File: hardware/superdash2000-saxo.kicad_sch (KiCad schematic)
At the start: 3 parts

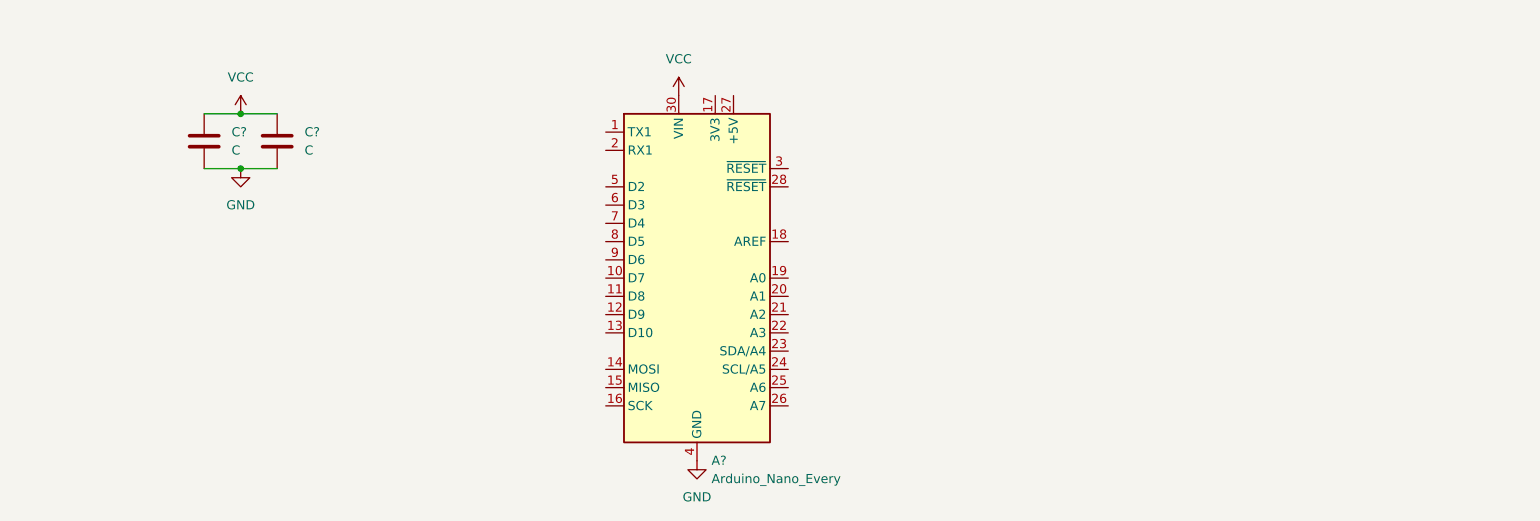
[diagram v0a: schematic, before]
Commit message: hardware: Add LDO and modify PCB
Signed-off-by: Thomas Antonini <antonini.thomas@gmail.com>
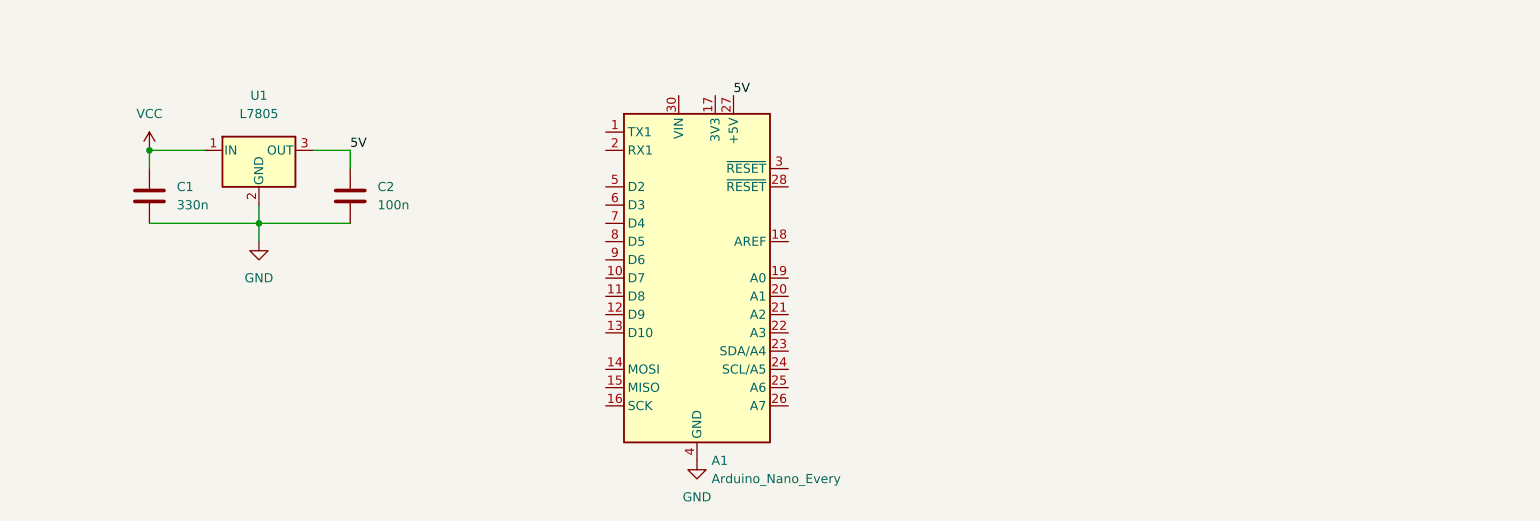
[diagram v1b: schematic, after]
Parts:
- removed C?: C, symbol Device:C
- added C2: 100n, Capacitor_THT:C_Disc_D3.0mm_W1.6mm_P2.50mm, symbol Device:C
- added U1: L7805, Package_TO_SOT_THT:TO-220-3_Vertical, symbol Regulator_Linear:L7805
- C1: renamed from C?; value C -> 330n; footprint (none) -> Capacitor_THT:C_Disc_D3.0mm_W1.6mm_P2.50mm
- gave numbers to parts that had none: 1
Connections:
- net GND: now also C2.2, U1.2 (GND)
- net VCC: now also U1.1 (IN); no longer A1.30 (VIN)
- net 5V: now reaches A1.27 (+5V)
- net 5V: now also C2.1, U1.3 (OUT)
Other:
- moved on the sheet: C1
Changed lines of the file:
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@@
 (kicad_sch (version 20211123) (generator eeschema)
   (paper "A4")
-  (junction (at 59.69 54.61) (diameter 0) (color 0 0 0 0)
+  (junction (at 46.99 59.69) (diameter 0) (color 0 0 0 0)
   )
-  (junction (at 59.69 62.23) (diameter 0) (color 0 0 0 0)
+  (junction (at 62.23 69.85) (diameter 0) (color 0 0 0 0)
   )
-  (wire (pts (xy 54.61 62.23) (xy 59.69 62.23))
+  (wire (pts (xy 62.23 69.85) (xy 62.23 72.39))
     (stroke (width 0) (type default) (color 0 0 0 0))
   )
-  (wire (pts (xy 59.69 62.23) (xy 64.77 62.23))
+  (wire (pts (xy 62.23 69.85) (xy 74.93 69.85))
     (stroke (width 0) (type default) (color 0 0 0 0))
   )
-  (wire (pts (xy 59.69 54.61) (xy 64.77 54.61))
+  (wire (pts (xy 62.23 67.31) (xy 62.23 69.85))
     (stroke (width 0) (type default) (color 0 0 0 0))
   )
-  (wire (pts (xy 54.61 54.61) (xy 59.69 54.61))
+  (wire (pts (xy 46.99 69.85) (xy 62.23 69.85))
     (stroke (width 0) (type default) (color 0 0 0 0))
+  )
+  (wire (pts (xy 74.93 59.69) (xy 69.85 59.69))
+    (stroke (width 0) (type default) (color 0 0 0 0))
+  )
+  (wire (pts (xy 74.93 62.23) (xy 74.93 59.69))
+    (stroke (width 0) (type default) (color 0 0 0 0))
+  )
+  (wire (pts (xy 46.99 59.69) (xy 54.61 59.69))
+    (stroke (width 0) (type default) (color 0 0 0 0))
+  )
+  (wire (pts (xy 46.99 59.69) (xy 46.99 62.23))
+    (stroke (width 0) (type default) (color 0 0 0 0))
+  )
+  (label "5V" (at 74.93 59.69 0)
+    (effects (font (size 1.27 1.27)) (justify left bottom))
+  )
+  (label "5V" (at 128.27 52.07 0)
+    (effects (font (size 1.27 1.27)) (justify left bottom))
   )
   (symbol (lib_id "power:GND") (at 123.19 102.87 0) (unit 1)
     (in_bom yes) (on_board yes) (fields_autoplaced)
-    (property "Reference" "#PWR?" (id 0) (at 123.19 109.22 0)
+    (property "Reference" "#PWR0101" (id 0) (at 123.19 109.22 0)
       (effects (font (size 1.27 1.27)) hide)
     )
@@
     (pin "1")
   )
-  (symbol (lib_id "power:GND") (at 59.69 62.23 0) (unit 1)
+  (symbol (lib_id "power:GND") (at 62.23 72.39 0) (unit 1)
     (in_bom yes) (on_board yes) (fields_autoplaced)
-    (property "Reference" "#PWR?" (id 0) (at 59.69 68.58 0)
+    (property "Reference" "#PWR0102" (id 0) (at 62.23 78.74 0)
       (effects (font (size 1.27 1.27)) hide)
     )
-    (property "Value" "GND" (id 1) (at 59.69 67.31 0))
-    (property "Footprint" "" (id 2) (at 59.69 62.23 0)
+    (property "Value" "GND" (id 1) (at 62.23 77.47 0))
+    (property "Footprint" "" (id 2) (at 62.23 72.39 0)
       (effects (font (size 1.27 1.27)) hide)
     )
-    (property "Datasheet" "" (id 3) (at 59.69 62.23 0)
+    (property "Datasheet" "" (id 3) (at 62.23 72.39 0)
       (effects (font (size 1.27 1.27)) hide)
     )
     (pin "1")
   )
-  (symbol (lib_id "Device:C") (at 64.77 58.42 0) (unit 1)
-    (in_bom yes) (on_board yes) (fields_autoplaced)
-    (property "Reference" "C?" (id 0) (at 68.58 57.1499 0)
+  (symbol (lib_id "Device:C") (at 74.93 66.04 0) (unit 1)
+    (in_bom yes) (on_board yes)
+    (property "Reference" "C2" (id 0) (at 78.74 64.7699 0)
       (effects (font (size 1.27 1.27)) (justify left))
     )
-    (property "Value" "C" (id 1) (at 68.58 59.6899 0)
+    (property "Value" "100n" (id 1) (at 78.74 67.3099 0)
       (effects (font (size 1.27 1.27)) (justify left))
     )
-    (property "Footprint" "" (id 2) (at 65.7352 62.23 0)
+    (property "Footprint" "Capacitor_THT:C_Disc_D3.0mm_W1.6mm_P2.50mm" (id 2) (at 75.8952 69.85 0)
       (effects (font (size 1.27 1.27)) hide)
     )
-    (property "Datasheet" "~" (id 3) (at 64.77 58.42 0)
+    (property "Datasheet" "~" (id 3) (at 74.93 66.04 0)
       (effects (font (size 1.27 1.27)) hide)
     )
@@
     (pin "2")
   )
+  (symbol (lib_id "Regulator_Linear:L7805") (at 62.23 59.69 0) (unit 1)
+    (in_bom yes) (on_board yes) (fields_autoplaced)
+    (property "Reference" "U1" (id 0) (at 62.23 52.07 0))
+    (property "Value" "L7805" (id 1) (at 62.23 54.61 0))
+    (property "Footprint" "Package_TO_SOT_THT:TO-220-3_Vertical" (id 2) (at 62.865 63.5 0)
+      (effects (font (size 1.27 1.27) italic) (justify left) hide)
+    )
+    (property "Datasheet" "http://www.st.com/content/ccc/resource/technical/document/datasheet/41/4f/b3/b0/12/d4/47/88/CD00000444.pdf/files/CD00000444.pdf/jcr:content/translations/en.CD00000444.pdf" (id 3) (at 62.23 60.96 0)
+      (effects (font (size 1.27 1.27)) hide)
+    )
+    (pin "1")
+    (pin "2")
+    (pin "3")
+  )
   (symbol (lib_id "MCU_Module:Arduino_Nano_Every") (at 123.19 77.47 0) (unit 1)
     (in_bom yes) (on_board yes) (fields_autoplaced)
-    (property "Reference" "A?" (id 0) (at 125.2094 102.87 0)
+    (property "Reference" "A1" (id 0) (at 125.2094 102.87 0)
       (effects (font (size 1.27 1.27)) (justify left))
     )
@@
     (pin "9")
   )
-  (symbol (lib_id "power:VCC") (at 120.65 52.07 0) (unit 1)
-    (in_bom yes) (on_board yes) (fields_autoplaced)
-    (property "Reference" "#PWR?" (id 0) (at 120.65 55.88 0)
+  (symbol (lib_id "Device:C") (at 46.99 66.04 0) (unit 1)
+    (in_bom yes) (on_board yes)
+    (property "Reference" "C1" (id 0) (at 50.8 64.7699 0)
+      (effects (font (size 1.27 1.27)) (justify left))
+    )
+    (property "Value" "330n" (id 1) (at 50.8 67.3099 0)
+      (effects (font (size 1.27 1.27)) (justify left))
+    )
+    (property "Footprint" "Capacitor_THT:C_Disc_D3.0mm_W1.6mm_P2.50mm" (id 2) (at 47.9552 69.85 0)
       (effects (font (size 1.27 1.27)) hide)
     )
-    (property "Value" "VCC" (id 1) (at 120.65 46.99 0))
-    (property "Footprint" "" (id 2) (at 120.65 52.07 0)
-      (effects (font (size 1.27 1.27)) hide)
-    )
-    (property "Datasheet" "" (id 3) (at 120.65 52.07 0)
-      (effects (font (size 1.27 1.27)) hide)
-    )
-    (pin "1")
-  )
-  (symbol (lib_id "Device:C") (at 54.61 58.42 0) (unit 1)
-    (in_bom yes) (on_board yes) (fields_autoplaced)
-    (property "Reference" "C?" (id 0) (at 58.42 57.1499 0)
-      (effects (font (size 1.27 1.27)) (justify left))
-    )
-    (property "Value" "C" (id 1) (at 58.42 59.6899 0)
-      (effects (font (size 1.27 1.27)) (justify left))
-    )
-    (property "Footprint" "" (id 2) (at 55.5752 62.23 0)
-      (effects (font (size 1.27 1.27)) hide)
-    )
-    (property "Datasheet" "~" (id 3) (at 54.61 58.42 0)
+    (property "Datasheet" "~" (id 3) (at 46.99 66.04 0)
       (effects (font (size 1.27 1.27)) hide)
     )
@@
     (pin "2")
   )
-  (symbol (lib_id "power:VCC") (at 59.69 54.61 0) (unit 1)
+  (symbol (lib_id "power:VCC") (at 46.99 59.69 0) (unit 1)
     (in_bom yes) (on_board yes) (fields_autoplaced)
-    (property "Reference" "#PWR?" (id 0) (at 59.69 58.42 0)
+    (property "Reference" "#PWR0103" (id 0) (at 46.99 63.5 0)
       (effects (font (size 1.27 1.27)) hide)
     )
-    (property "Value" "VCC" (id 1) (at 59.69 49.53 0))
-    (property "Footprint" "" (id 2) (at 59.69 54.61 0)
+    (property "Value" "VCC" (id 1) (at 46.99 54.61 0))
+    (property "Footprint" "" (id 2) (at 46.99 59.69 0)
       (effects (font (size 1.27 1.27)) hide)
     )
-    (property "Datasheet" "" (id 3) (at 59.69 54.61 0)
+    (property "Datasheet" "" (id 3) (at 46.99 59.69 0)
       (effects (font (size 1.27 1.27)) hide)
     )
@@
   (symbol_instances
     (path "/091fa7fe-31f2-4bc7-b9ae-103378e7ecef"
-      (reference "#PWR?") (unit 1) (value "GND") (footprint "")
+      (reference "#PWR0101") (unit 1) (value "GND") (footprint "")
     )
     (path "/2d42965a-3076-4350-a25e-4a3c6a2ed82a"
-      (reference "#PWR?") (unit 1) (value "GND") (footprint "")
-    )
-    (path "/c516dcf8-f4c1-4011-b67e-724a30d35ccf"
-      (reference "#PWR?") (unit 1) (value "VCC") (footprint "")
+      (reference "#PWR0102") (unit 1) (value "GND") (footprint "")
     )
     (path "/f16717c9-4da6-4641-a01d-d15d2a023c10"
-      (reference "#PWR?") (unit 1) (value "VCC") (footprint "")
+      (reference "#PWR0103") (unit 1) (value "VCC") (footprint "")
     )
     (path "/65c02b6a-4170-4a63-9193-eec01920d5e8"
-      (reference "A?") (unit 1) (value "Arduino_Nano_Every") (footprint "Module:Arduino_Nano")
-    )
-    (path "/4f6c1128-a97e-4ba7-b96b-87bbab886b6c"
-      (reference "C?") (unit 1) (value "C") (footprint "")
+      (reference "A1") (unit 1) (value "Arduino_Nano_Every") (footprint "Module:Arduino_Nano")
     )
     (path "/eae34f3b-9c4a-4c30-981e-9737d2460a8b"
-      (reference "C?") (unit 1) (value "C") (footprint "")
+      (reference "C1") (unit 1) (value "330n") (footprint "Capacitor_THT:C_Disc_D3.0mm_W1.6mm_P2.50mm")
+    )
+    (path "/42e4bc1f-a2a4-4278-9288-7ff8c44f13b1"
+      (reference "C2") (unit 1) (value "100n") (footprint "Capacitor_THT:C_Disc_D3.0mm_W1.6mm_P2.50mm")
+    )
+    (path "/4dcd0dda-1663-4b04-85dd-f6fe52c14280"
+      (reference "U1") (unit 1) (value "L7805") (footprint "Package_TO_SOT_THT:TO-220-3_Vertical")
     )
   )

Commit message: hardware: Update schematics
Add fuse
Add 3-pin jumper
Add molex connector
Move symbols position

Signed-off-by: Thomas Antonini <antonini.thomas@gmail.com>
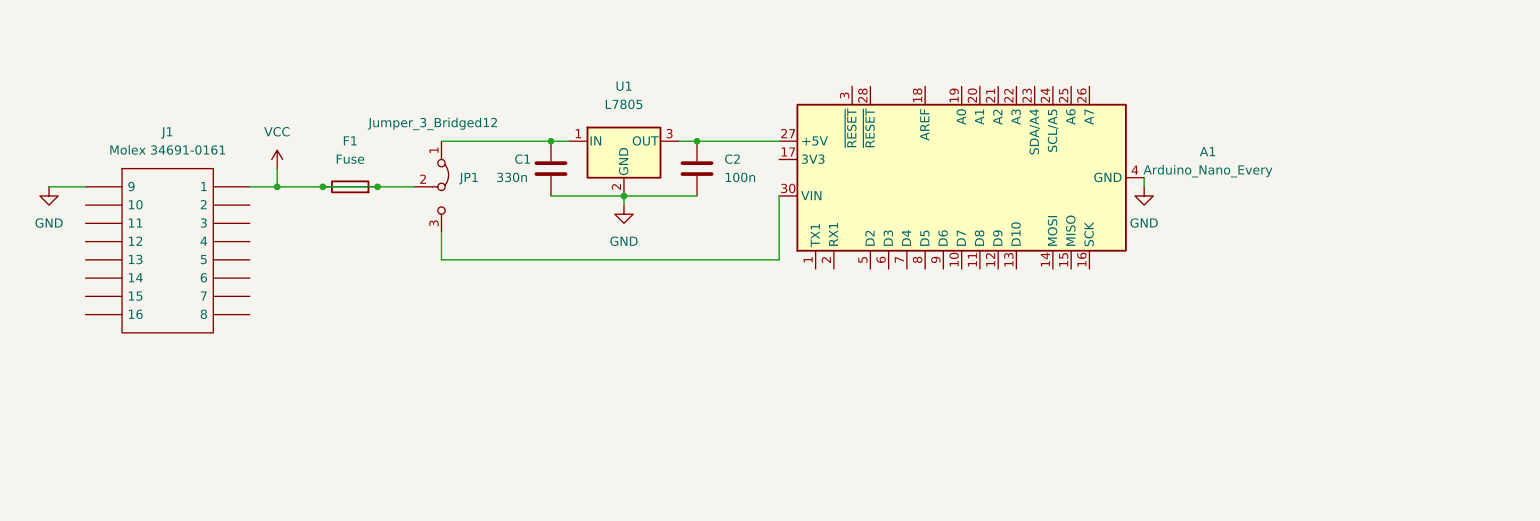
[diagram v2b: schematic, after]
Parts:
- added F1: Fuse, symbol Device:Fuse
- added J1: Molex 34691-0161, Molex_34691-0161:Molex 34691-0161, symbol Molex_34691-0161:Molex 34691-0161
- added JP1: Jumper_3_Bridged12, symbol Jumper:Jumper_3_Bridged12
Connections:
- net GND: now also J1.9
- net VCC: now also F1.1, F1.2, J1.1, JP1.2 (C); no longer C1.1, U1.1 (IN)
- net at A1.30 (VIN): now also JP1.3 (B)
- net 5V: no longer names the net of A1.27 (+5V), C2.1, U1.3 (OUT)
- new net: C1.1, JP1.1 (A), U1.1 (IN)
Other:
- moved on the sheet: A1, C1, C2, U1
